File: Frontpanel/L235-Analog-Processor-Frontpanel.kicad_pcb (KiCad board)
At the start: 2 copper layers, 60 x 128.5 mm, 0 parts

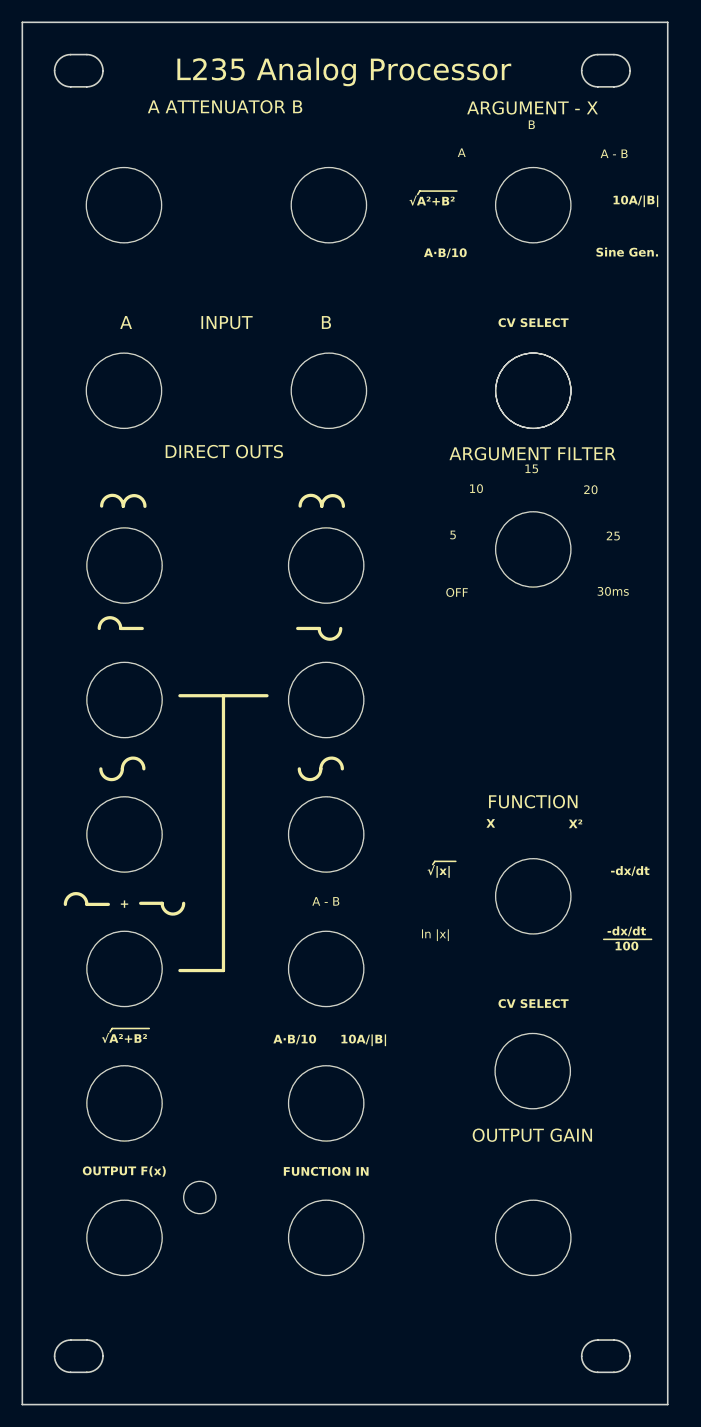
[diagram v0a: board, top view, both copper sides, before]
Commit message: Added leds selectors
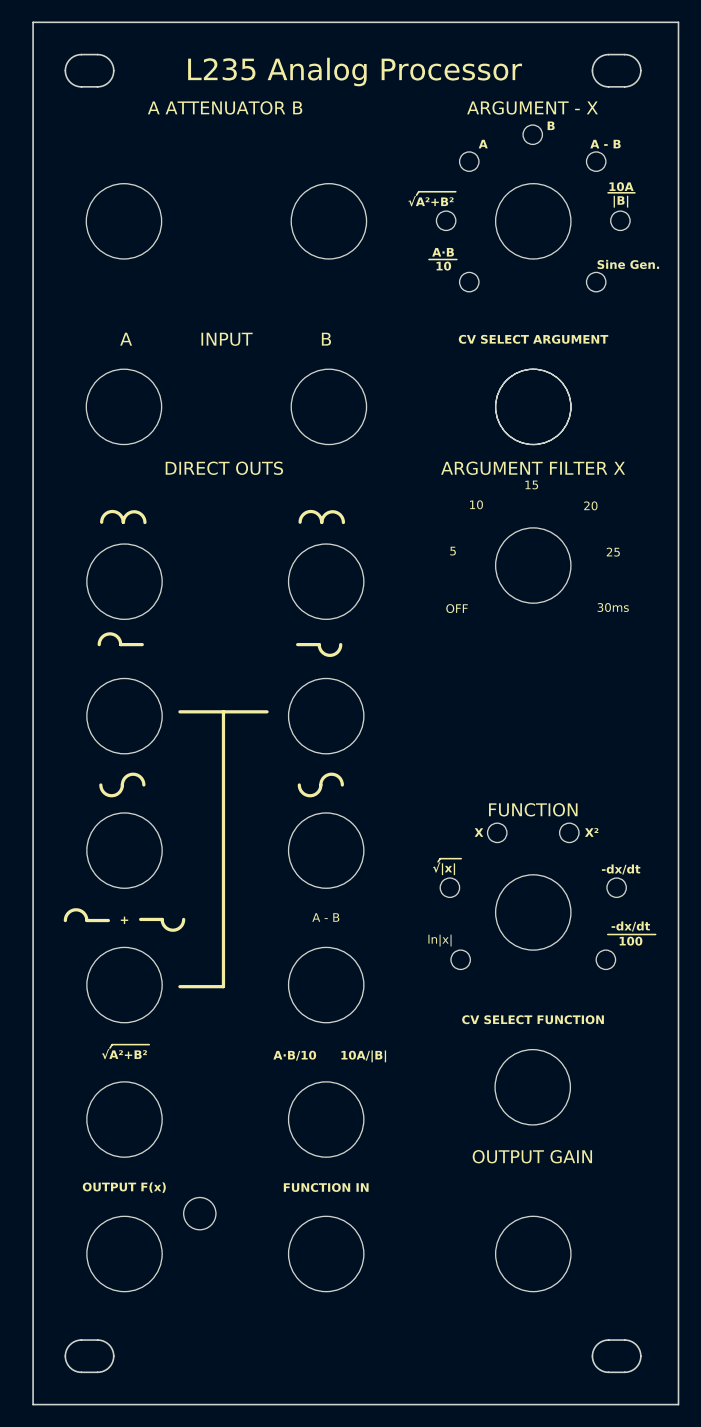
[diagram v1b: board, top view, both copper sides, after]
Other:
- outline, holes or cut-outs redrawn
- board text added: "10A |B|"
- board text added: "ARGUMENT FILTER X"
- board text added: "A·B 10"
- board text added: "CV SELECT ARGUMENT"
- board text added: "CV SELECT FUNCTION"
- board text added: "ln|x|"
- board text removed: "ARGUMENT FILTER"
- board text removed: "CV SELECT"
- board text removed: "ln |x|"
